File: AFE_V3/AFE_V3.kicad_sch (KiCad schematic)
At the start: 1 part, among them U1 STM32F407ZETx

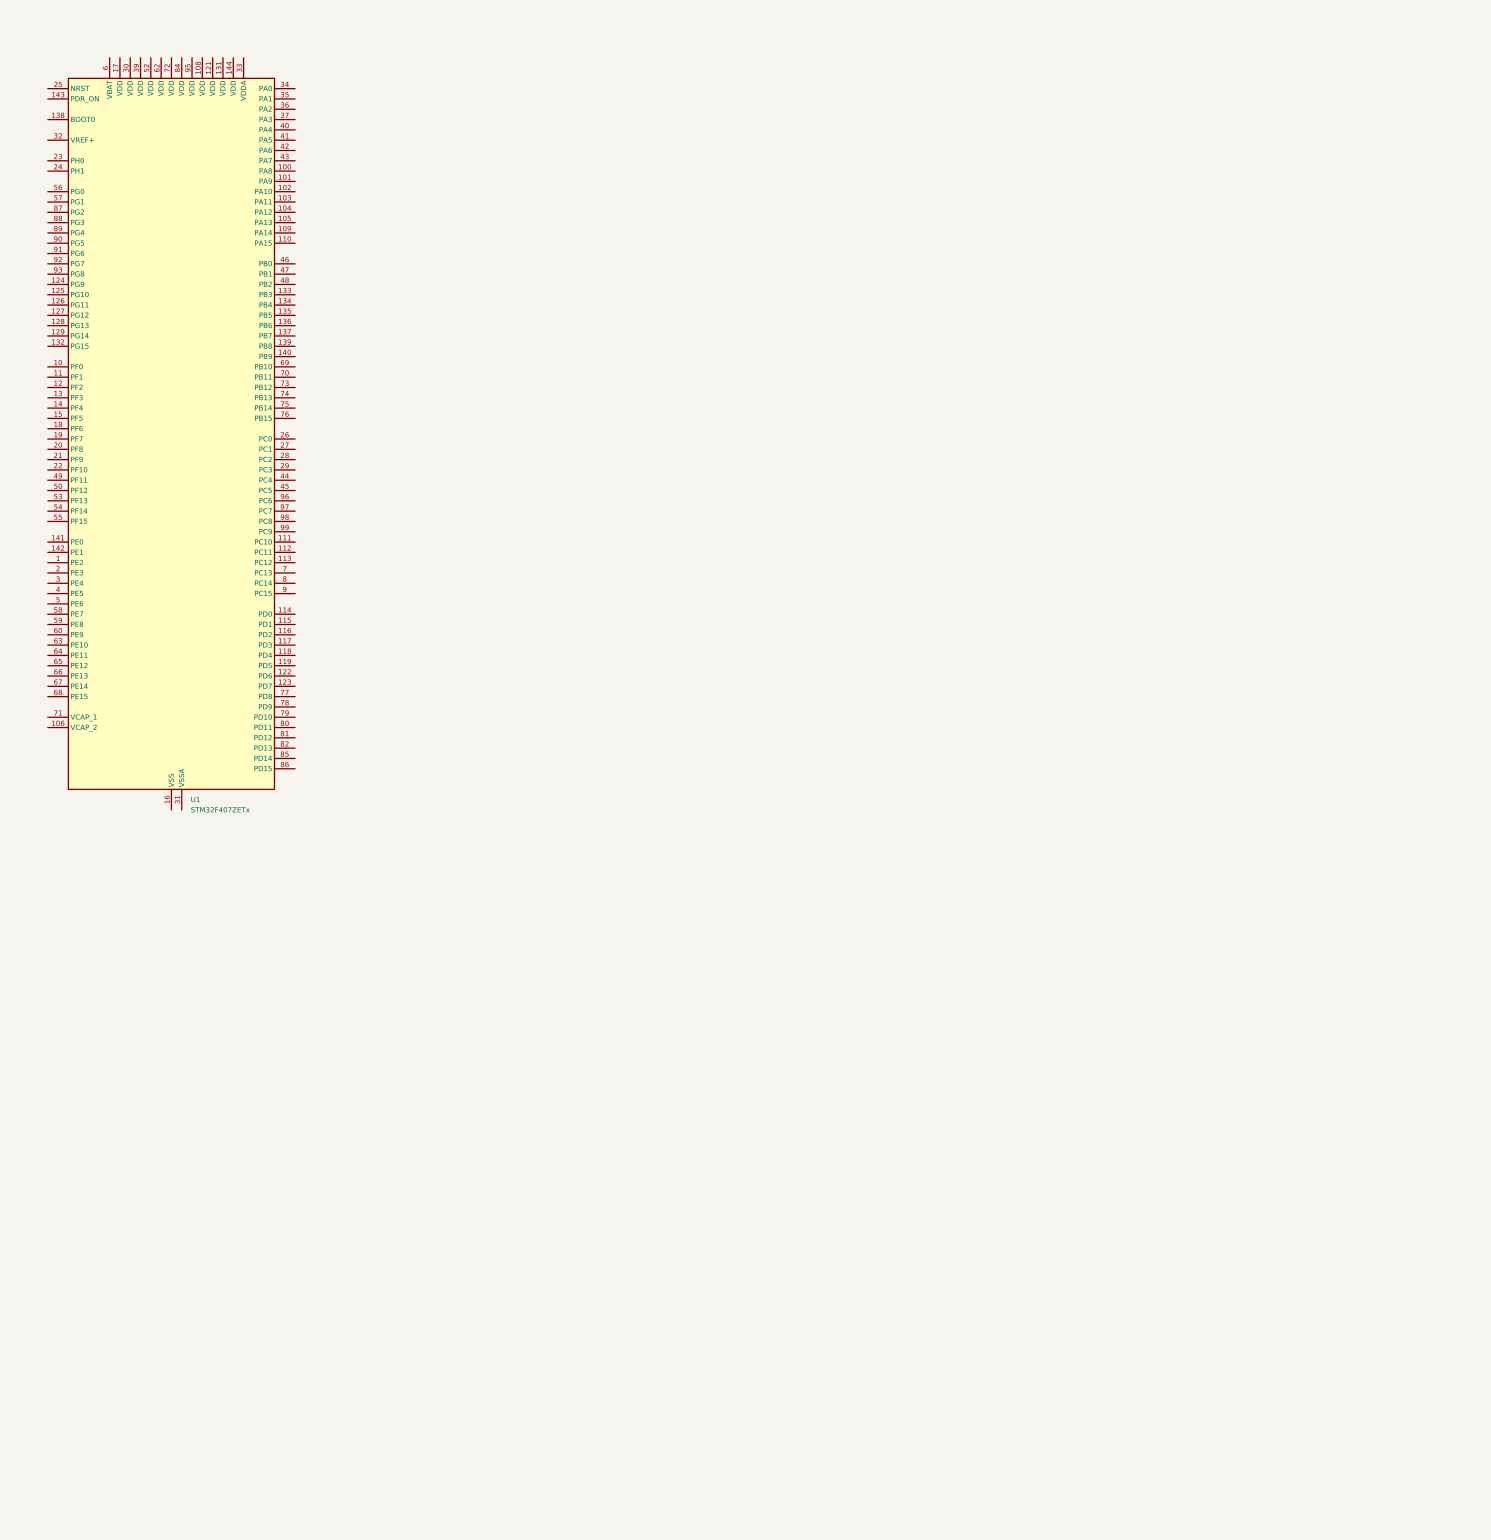
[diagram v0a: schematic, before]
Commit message: Added new files:lib and pcb
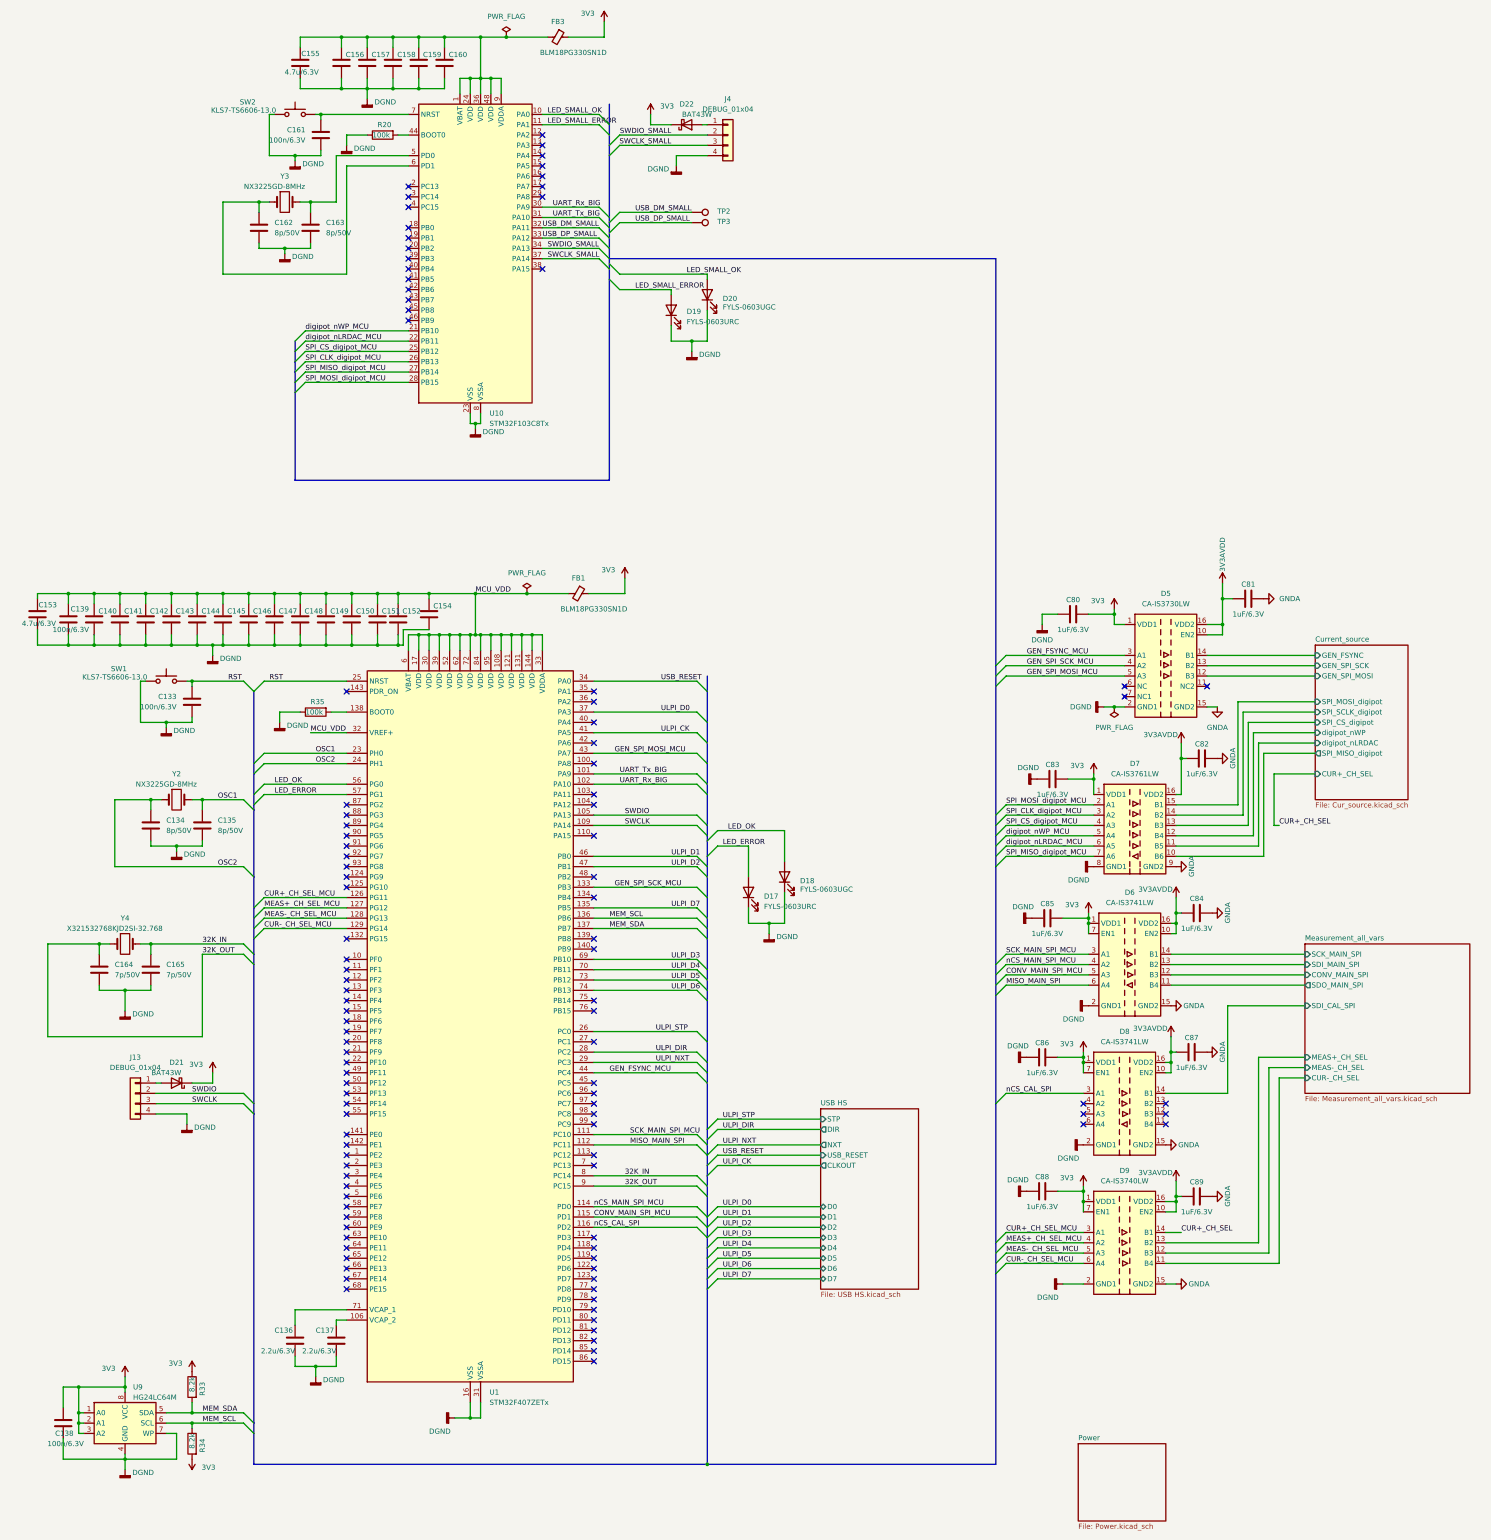
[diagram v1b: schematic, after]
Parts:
- added C133, C138, C139, C140, C141, C142, C143, C144, C145, C146, C147, C148, C149, C150, C151, C152, C154, C156, C157, C158, C159, C160, C161: 100n/6.3V, Capacitor_SMD:C_0402_1005Metric, symbol Device:C
- added C134, C135, C162, C163: 8p/50V, Capacitor_SMD:C_0603_1608Metric_Pad1.08x0.95mm_HandSolder, symbol Device:C
- added C136, C137: 2.2u/6.3V, Capacitor_SMD:C_0805_2012Metric_Pad1.18x1.45mm_HandSolder, symbol Device:C
- added C153, C155: 4.7u/6.3V, Capacitor_SMD:C_0805_2012Metric_Pad1.18x1.45mm_HandSolder, symbol Device:C
- added C164, C165: 7p/50V, Capacitor_SMD:C_0603_1608Metric_Pad1.08x0.95mm_HandSolder, symbol Device:C
- added C80, C81, C82, C83, C84, C85, C86, C87, C88, C89: 1uF/6.3V, Capacitor_SMD:C_0603_1608Metric_Pad1.08x0.95mm_HandSolder, symbol Device:C
- added D17, D19: FYLS-0603URC, LED_SMD:LED_0603_1608Metric_Pad1.05x0.95mm_HandSolder, symbol Device:LED
- added D18, D20: FYLS-0603UGC, LED_SMD:LED_0603_1608Metric_Pad1.05x0.95mm_HandSolder, symbol Device:LED
- added D21, D22: BAT43W, Diode_SMD:D_SOD-123, symbol Device:D_Schottky
- added D5: CA-IS3730LW, Package_SO:SOIC-16W_7.5x10.3mm_P1.27mm, symbol zpc-lib:CA-IS3730LW
- added D6, D8: CA-IS3741LW, Package_SO:SOIC-16W_7.5x10.3mm_P1.27mm, symbol zpc-lib:CA-IS3741LW
- added D7: CA-IS3761LW, Package_SO:SOIC-16W_7.5x10.3mm_P1.27mm, symbol zpc-lib:CA-IS3761LW
- added D9: CA-IS3740LW, Package_SO:SOIC-16W_7.5x10.3mm_P1.27mm, symbol zpc-lib:CA-IS3740LW
- added FB1, FB3: BLM18PG330SN1D, Inductor_SMD:L_0603_1608Metric_Pad1.05x0.95mm_HandSolder, symbol Device:FerriteBead_Small
- added J13, J4: DEBUG_01x04, Connector_PinHeader_2.54mm:PinHeader_1x04_P2.54mm_Vertical, symbol Connector_Generic:Conn_01x04
- added R20, R35: 100k, Resistor_SMD:R_0603_1608Metric_Pad0.98x0.95mm_HandSolder, symbol Device:R
- added R33, R34: 8.2k, Resistor_SMD:R_0603_1608Metric_Pad0.98x0.95mm_HandSolder, symbol Device:R
- added SW1, SW2: KLS7-TS6606-13.0, Button_Switch_THT:SW_PUSH_6mm_H4.3mm, symbol Switch:SW_Push
- added TP2, TP3: ~, TestPoint:TestPoint_Pad_D1.0mm, symbol Connector:TestPoint
- added U10: STM32F103C8Tx, Package_QFP:LQFP-48_7x7mm_P0.5mm, symbol MCU_ST_STM32F1:STM32F103C8Tx
- added U9: HG24LC64M, Package_SO:SOIC-8_3.9x4.9mm_P1.27mm, symbol Memory_EEPROM:24LC32
- added Y2, Y3: NX3225GD-8MHz, zpc-lib:NX3225GD, symbol Device:Crystal
- added Y4: X321532768KJD2SI-32.768, Crystal:Crystal_SMD_3215-2Pin_3.2x1.5mm, symbol Device:Crystal
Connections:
- net UART_Tx_BIG: now reaches U1.101 (PA9)
- net UART_Tx_BIG: now also U10.31 (PA10)
- net UART_Rx_BIG: now reaches U1.102 (PA10)
- net UART_Rx_BIG: now also U10.30 (PA9)
- net SWDIO: now reaches U1.105 (PA13)
- net SWDIO: now also J13.2 (Pin_2)
- net at U1.106 (VCAP_2): now also C137.1
- net DGND: now reaches U1.107 (VSS), U1.120 (VSS), U1.130 (VSS), U1.16 (VSS), U1.38 (VSS), U1.51 (VSS), U1.61 (VSS), U1.83 (VSS), U1.94 (VSS)
- net DGND: now also U1.31 (VSSA), C133.1, C134.1, C135.1, C136.2, C137.2, C138.1, C139.1, C140.1, C141.1, C142.1, C143.1, C144.1, C145.1, C146.1, C147.1, C148.1, C149.1, C150.1, C151.1, C152.1, C153.2, C154.1, C155.2, C156.1, C157.1, C158.1, C159.1, C160.1, C161.1, C162.1, C163.1, C164.1, C165.1, C80.1, C83.1, C85.1, C86.1, C88.1, D17.1 (K), D18.1 (K), D19.1 (K), D20.1 (K), D5.2 (GND1), D5.8 (GND1), D6.2 (GND1), D6.8 (GND1), D7.8 (GND1), D8.2 (GND1), D8.8 (GND1), D9.2 (GND1), D9.8 (GND1), J13.4 (Pin_4), J4.4 (Pin_4), R20.1, R35.1, SW1.1, SW2.1, U10.23 (VSS), U10.35 (VSS), U10.47 (VSS), U10.8 (VSSA), U9.4 (GND), U9.7 (WP)
- net MCU_VDD: now reaches U1.108 (VDD)
- net MCU_VDD: now also U1.121 (VDD), U1.131 (VDD), U1.144 (VDD), U1.17 (VDD), U1.30 (VDD), U1.32 (VREF+), U1.33 (VDDA), U1.39 (VDD), U1.52 (VDD), U1.6 (VBAT), U1.62 (VDD), U1.72 (VDD), U1.84 (VDD), U1.95 (VDD), C139.2, C140.2, C141.2, C142.2, C143.2, C144.2, C145.2, C146.2, C147.2, C148.2, C149.2, C150.2, C151.2, C152.2, C153.1, C154.2, FB1.2
- net SWCLK: now reaches U1.109 (PA14)
- net SWCLK: now also J13.3 (Pin_3)
- net SCK_MAIN_SPI_MCU: now reaches U1.111 (PC10)
- net SCK_MAIN_SPI_MCU: now also D6.3 (A1)
- net MISO_MAIN_SPI: now reaches U1.112 (PC11)
- net MISO_MAIN_SPI: now also D6.6 (A4)
- net nCS_MAIN_SPI_MCU: now reaches U1.114 (PD0)
- net nCS_MAIN_SPI_MCU: now also D6.4 (A2)
- net CONV_MAIN_SPI_MCU: now reaches U1.115 (PD1)
- net CONV_MAIN_SPI_MCU: now also D6.5 (A3)
- net nCS_CAL_SPI: now reaches U1.116 (PD2)
- net nCS_CAL_SPI: now also D8.3 (A1)
- net CUR+_CH_SEL_MCU: now reaches U1.126 (PG11)
- net CUR+_CH_SEL_MCU: now also D9.3 (A1)
- net MEAS+_CH_SEL_MCU: now reaches U1.127 (PG12)
- net MEAS+_CH_SEL_MCU: now also D9.4 (A2)
- net MEAS-_CH_SEL_MCU: now reaches U1.128 (PG13)
- net MEAS-_CH_SEL_MCU: now also D9.5 (A3)
- net CUR-_CH_SEL_MCU: now reaches U1.129 (PG14)
- net CUR-_CH_SEL_MCU: now also D9.6 (A4)
- net GEN_SPI_SCK_MCU: now reaches U1.133 (PB3)
- net GEN_SPI_SCK_MCU: now also D5.4 (A2)
- net ULPI_D7: now reaches U1.135 (PB5)
- net MEM_SCL: now reaches U1.136 (PB6)
- net MEM_SCL: now also R34.1, U9.6 (SCL)
- net MEM_SDA: now reaches U1.137 (PB7)
- net MEM_SDA: now also R33.2, U9.5 (SDA)
- net at U1.138 (BOOT0): now also R35.2
- net OSC1: now reaches U1.23 (PH0)
- net OSC1: now also C135.2, Y2.2
- net OSC2: now reaches U1.24 (PH1)
- net OSC2: now also C134.2, Y2.1
- net RST: now reaches U1.25 (NRST)
- net RST: now also C133.2, SW1.2
- net ULPI_STP: now reaches U1.26 (PC0)
- net ULPI_DIR: now reaches U1.28 (PC2)
- net ULPI_NXT: now reaches U1.29 (PC3)
- net USB_RESET: now reaches U1.34 (PA0)
- net ULPI_D0: now reaches U1.37 (PA3)
- net ULPI_CK: now reaches U1.41 (PA5)
- net GEN_SPI_MOSI_MCU: now reaches U1.43 (PA7)
- net GEN_SPI_MOSI_MCU: now also D5.5 (A3)
- net GEN_FSYNC_MCU: now reaches U1.44 (PC4)
- net GEN_FSYNC_MCU: now also D5.3 (A1)
- net ULPI_D1: now reaches U1.46 (PB0)
- net ULPI_D2: now reaches U1.47 (PB1)
- net LED_OK: now reaches U1.56 (PG0)
- net LED_OK: now also D18.2 (A)
- net LED_ERROR: now reaches U1.57 (PG1)
- net LED_ERROR: now also D17.2 (A)
- net ULPI_D3: now reaches U1.69 (PB10)
- net ULPI_D4: now reaches U1.70 (PB11)
- net at U1.71 (VCAP_1): now also C136.1
- net ULPI_D5: now reaches U1.73 (PB12)
- net ULPI_D6: now reaches U1.74 (PB13)
- net 32K_IN: now reaches U1.8 (PC14)
- net 32K_IN: now also C165.2, Y4.2
- net 32K_OUT: now reaches U1.9 (PC15)
- net 32K_OUT: now also C164.2, Y4.1
- new net: C161.2, SW2.2, U10.7 (NRST)
- new net: D22.2 (A), J4.1 (Pin_1)
- new net: C155.1, C156.2, C157.2, C158.2, C159.2, C160.2, FB3.2, U10.1 (VBAT), U10.24 (VDD), U10.36 (VDD), U10.48 (VDD), U10.9 (VDDA)
- new net: D21.2 (A), J13.1 (Pin_1)
- new net: R20.2, U10.44 (BOOT0)
- new net: C163.2, U10.5 (PD0), Y3.2
- new net: C162.2, U10.6 (PD1), Y3.1
- new net 3V3: C138.2, C80.2, C83.2, C85.2, C86.2, C88.2, D21.1 (K), D22.1 (K), D5.1 (VDD1), D6.1 (VDD1), D6.7 (EN1), D7.1 (VDD1), D8.1 (VDD1), D8.7 (EN1), D9.1 (VDD1), D9.7 (EN1), FB1.1, FB3.1, R33.1, R34.2, U9.1 (A0), U9.2 (A1), U9.3 (A2), U9.8 (VCC)
- new net 3V3AVDD: C81.1, C82.1, C84.1, C87.1, C89.1, D5.10 (EN2), D5.16 (VDD2), D6.10 (EN2), D6.16 (VDD2), D7.16 (VDD2), D8.10 (EN2), D8.16 (VDD2), D9.10 (EN2), D9.16 (VDD2)
- new net CUR+_CH_SEL: D9.14 (B1)
- new net Current_source/GEN_FSYNC: D5.14 (B1)
- new net Current_source/GEN_SPI_MOSI: D5.12 (B3)
- new net Current_source/GEN_SPI_SCK: D5.13 (B2)
- new net Current_source/SPI_CS_digipot: D7.13 (B3)
- new net Current_source/SPI_MISO_digipot: D7.10 (B6)
- new net Current_source/SPI_MOSI_digipot: D7.15 (B1)
- new net Current_source/SPI_SCLK_digipot: D7.14 (B2)
- new net Current_source/digipot_nLRDAC: D7.11 (B5)
- new net Current_source/digipot_nWP: D7.12 (B4)
- new net GNDA: C81.2, C82.2, C84.2, C87.2, C89.2, D5.15 (GND2), D5.9 (GND2), D6.15 (GND2), D6.9 (GND2), D7.9 (GND2), D8.15 (GND2), D8.9 (GND2), D9.15 (GND2), D9.9 (GND2)
- new net LED_SMALL_ERROR: D19.2 (A), U10.11 (PA1)
- new net LED_SMALL_OK: D20.2 (A), U10.10 (PA0)
- new net Measurement_all_vars/CONV_MAIN_SPI: D6.12 (B3)
- new net Measurement_all_vars/CUR-_CH_SEL: D9.11 (B4)
- new net Measurement_all_vars/MEAS+_CH_SEL: D9.13 (B2)
- new net Measurement_all_vars/MEAS-_CH_SEL: D9.12 (B3)
- new net Measurement_all_vars/SCK_MAIN_SPI: D6.14 (B1)
- new net Measurement_all_vars/SDI_CAL_SPI: D8.14 (B1)
- new net Measurement_all_vars/SDI_MAIN_SPI: D6.13 (B2)
- new net Measurement_all_vars/SDO_MAIN_SPI: D6.11 (B4)
- new net SPI_CLK_digipot_MCU: D7.3 (A2), U10.26 (PB13)
- new net SPI_CS_digipot_MCU: D7.4 (A3), U10.25 (PB12)
- new net SPI_MISO_digipot_MCU: D7.7 (A6), U10.27 (PB14)
- new net SPI_MOSI_digipot_MCU: D7.2 (A1), U10.28 (PB15)
- new net SWCLK_SMALL: J4.3 (Pin_3), U10.37 (PA14)
- new net SWDIO_SMALL: J4.2 (Pin_2), U10.34 (PA13)
- new net USB_DM_SMALL: TP2.1, U10.32 (PA11)
- new net USB_DP_SMALL: TP3.1, U10.33 (PA12)
- new net digipot_nLRDAC_MCU: D7.6 (A5), U10.22 (PB11)
- new net digipot_nWP_MCU: D7.5 (A4), U10.21 (PB10)
- no-connect marks 0 -> 108
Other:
- added sheet Current_source (Cur_source.kicad_sch)
- added sheet Measurement_all_vars (Measurement_all_vars.kicad_sch)
- added sheet Power (Power.kicad_sch)
- added sheet USB HS (USB HS.kicad_sch)
- moved on the sheet: U1

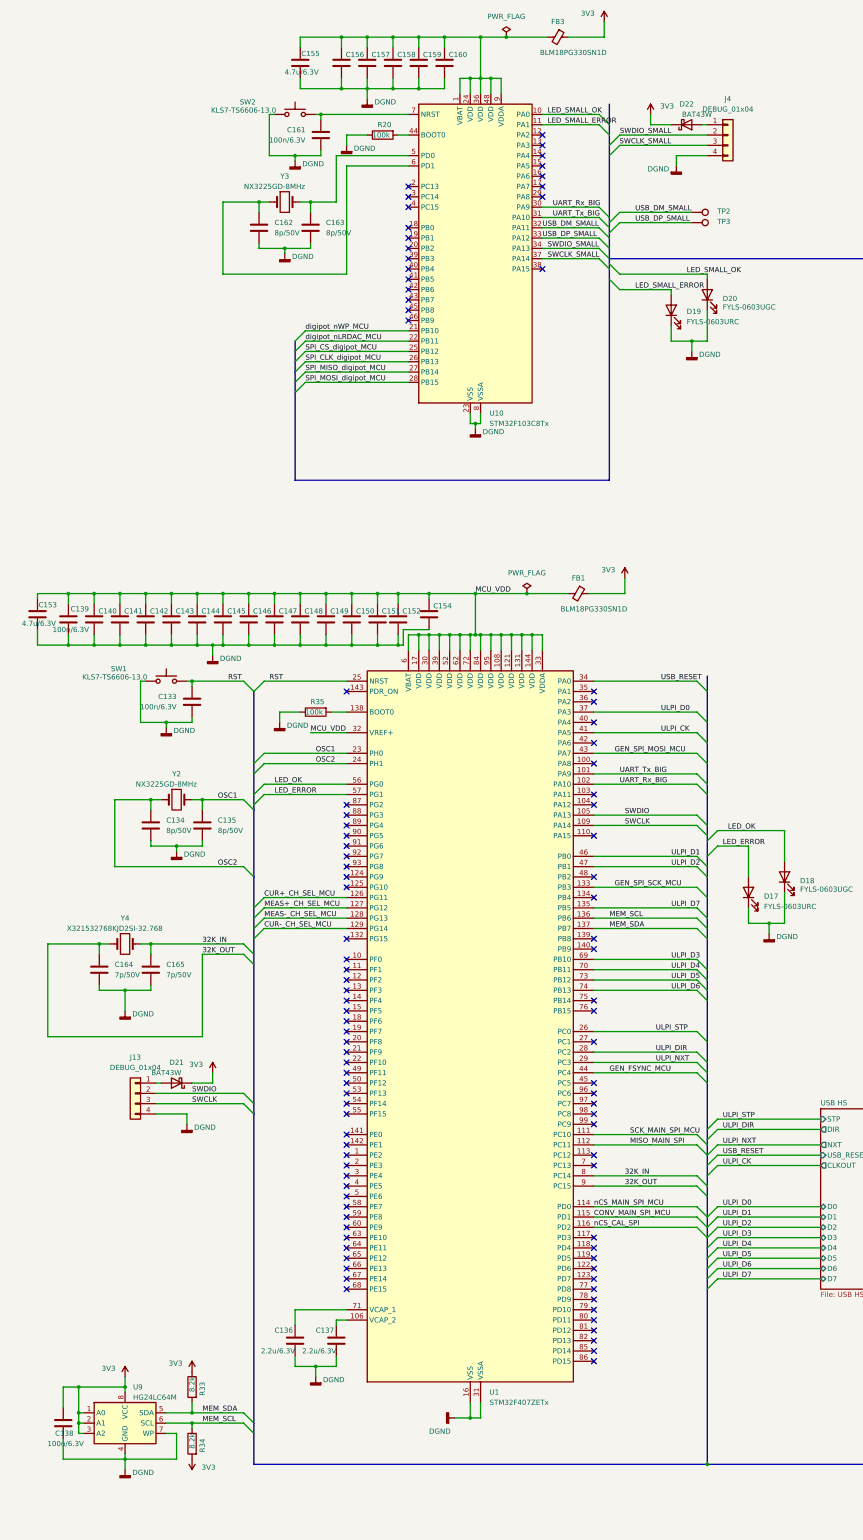
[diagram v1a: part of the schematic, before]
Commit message: PCB tracing in progress. Added some 3d models
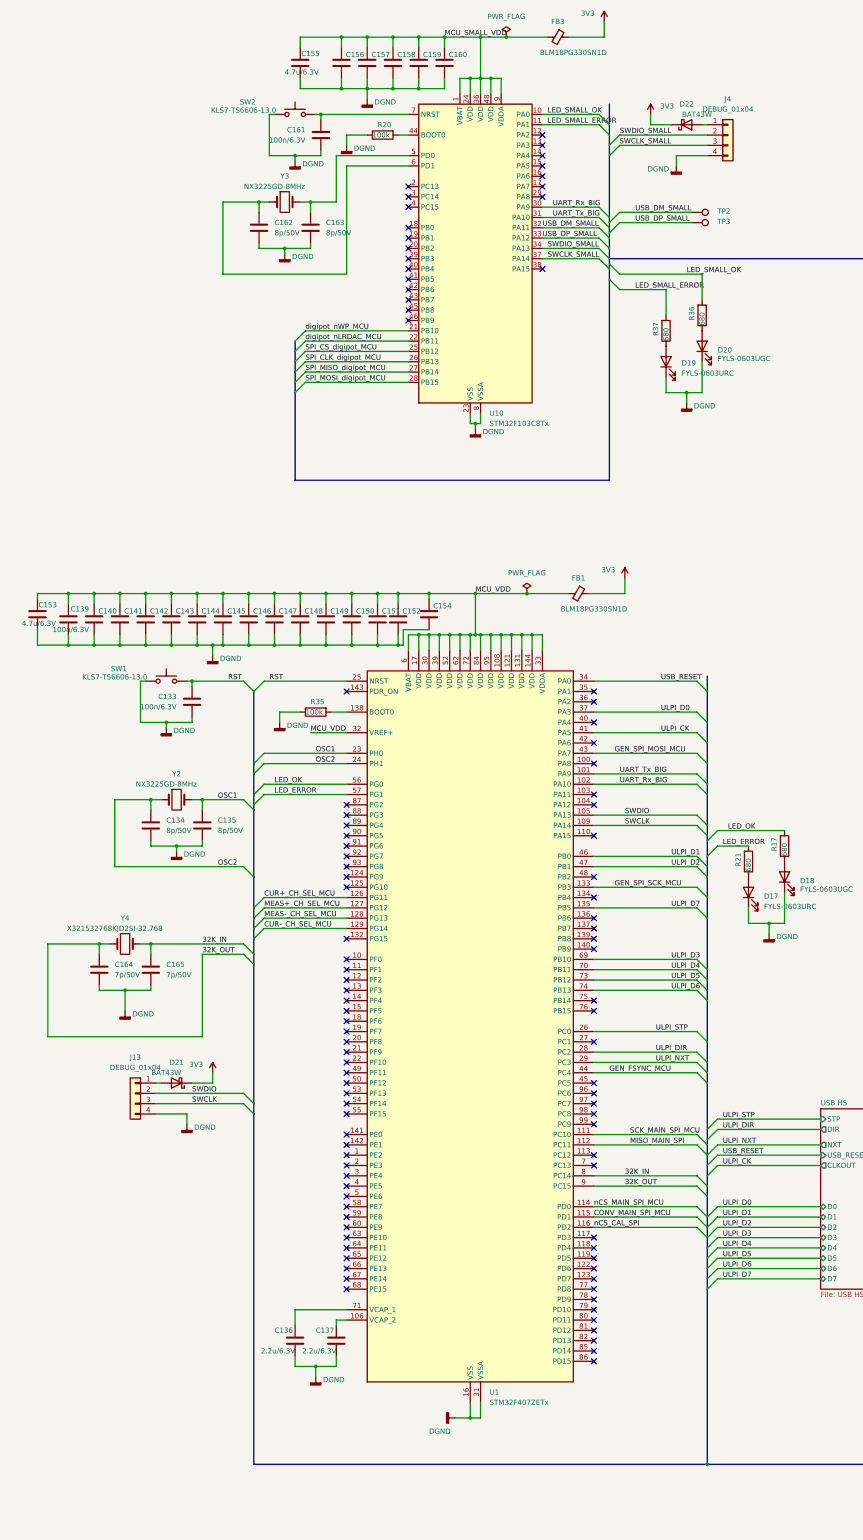
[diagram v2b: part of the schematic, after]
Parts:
- removed C138: 100n/6.3V, Capacitor_SMD:C_0402_1005Metric, symbol Device:C
- removed R33, R34: 8.2k, Resistor_SMD:R_0603_1608Metric_Pad0.98x0.95mm_HandSolder, symbol Device:R
- removed U9: HG24LC64M, Package_SO:SOIC-8_3.9x4.9mm_P1.27mm, symbol Memory_EEPROM:24LC32
- added R17, R21, R36, R37: 680, Resistor_SMD:R_0603_1608Metric_Pad0.98x0.95mm_HandSolder, symbol Device:R
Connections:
- net LED_ERROR: now also R21.2; no longer D17.2 (A)
- net LED_OK: now also R17.2; no longer D18.2 (A)
- net LED_SMALL_ERROR: now also R37.2; no longer D19.2 (A)
- net LED_SMALL_OK: now also R36.2; no longer D20.2 (A)
- net MCU_SMALL_VDD: now reaches C155.1, C156.2, C157.2, C158.2, C159.2, C160.2, FB3.2, U10.1 (VBAT), U10.24 (VDD), U10.36 (VDD), U10.48 (VDD), U10.9 (VDDA)
- net MEM_SCL: no longer names the net of U1.136 (PB6)
- net MEM_SDA: no longer names the net of U1.137 (PB7)
- new net: D18.2 (A), R17.1
- new net: D20.2 (A), R36.1
- new net: D17.2 (A), R21.1
- new net: D19.2 (A), R37.1
- no-connect marks 108 -> 110
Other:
- moved on the sheet: D19, D20

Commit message: PCB tracing in progress
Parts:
- added J1: Conn_2Rows-17Pins, Connector_PinHeader_2.54mm:PinHeader_2x08_P2.54mm_Horizontal, symbol Connector_Generic:Conn_2Rows-17Pins
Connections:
- net CUR+_CH_SEL_MCU: now also D9.6 (A4); no longer D9.3 (A1)
- net CUR-_CH_SEL_MCU: now also D9.3 (A1); no longer D9.6 (A4)
- net GNDA: now also J1.10 (Pin_10), J1.12 (Pin_12), J1.14 (Pin_14), J1.16 (Pin_16), J1.2 (Pin_2), J1.4 (Pin_4), J1.6 (Pin_6), J1.8 (Pin_8)
- net MEAS+_CH_SEL_MCU: now also D9.5 (A3); no longer D9.4 (A2)
- net MEAS-_CH_SEL_MCU: now also D9.4 (A2); no longer D9.5 (A3)
- new net cur+1: J1.1 (Pin_1)
- new net cur+2: J1.3 (Pin_3)
- new net cur-1: J1.15 (Pin_15)
- new net cur-2: J1.13 (Pin_13)
- new net imp+1: J1.7 (Pin_7)
- new net imp+2: J1.5 (Pin_5)
- new net imp-1: J1.11 (Pin_11)
- new net imp-2: J1.9 (Pin_9)
- no-connect marks 110 -> 111
